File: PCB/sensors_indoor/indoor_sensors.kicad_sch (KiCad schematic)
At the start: 31 parts, among them J3 B5B-ZR, Q1 DMN62D0U, U10 SPS30, U11 74LVC1G08, U4 LPS22DF, U5 SHT45-AD1F, U6 SCD41-D-R2, U7 SGP41, U8 OPT4001DNPRQ1, U9 TSOP38436

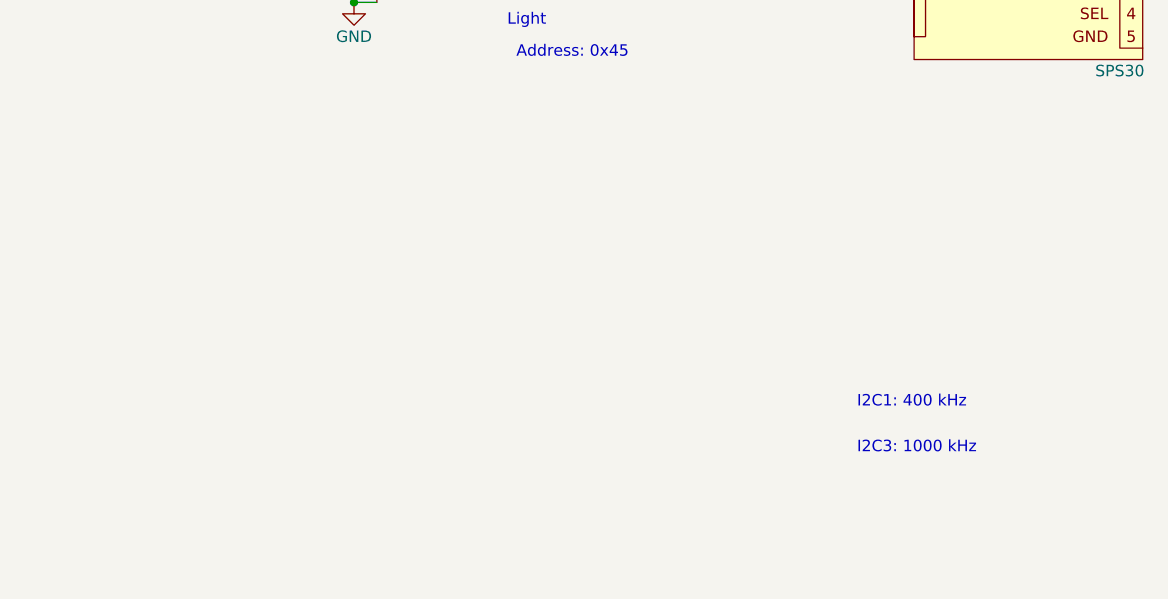
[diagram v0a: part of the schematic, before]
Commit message: Added UV sensor
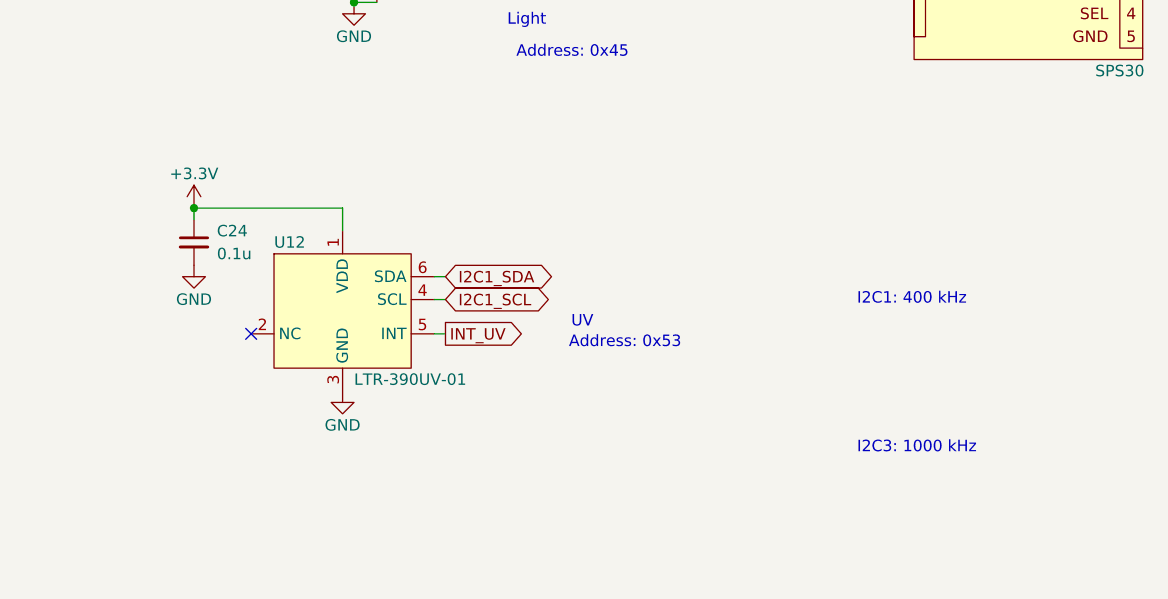
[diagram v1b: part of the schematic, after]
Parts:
- added C24: 0.1u, Capacitor_SMD:C_0402_1005Metric, symbol Device:C_Small
- added U12: LTR-390UV-01, DWlib:Liteon_LTR-390UV-01, symbol DWlib:LTR-390UV-01
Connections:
- net +3.3V: now also C24.1, U12.1 (VDD)
- net GND: now also C24.2, U12.3 (GND)
- net I2C1_SCL: now also U12.4 (SCL)
- net I2C1_SDA: now also U12.6 (SDA)
- new net INT_UV: U12.5 (INT)
- no-connect marks 1 -> 2
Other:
- note added: "Address: 0x53"
- note added: "UV"
